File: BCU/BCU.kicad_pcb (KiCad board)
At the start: 2 copper layers, 73 parts, among them IC1 STM32G474RET6, IC2 TJA1042T_3,118, IC3 LM317MDCYR, IC4 LTC6820HUD#PBF, IC5 LM2842YQMK_NOPB, IC6 LM5164DDAR, J1 JTAG Connector, J2 SM04B-PASS-TBT_LF__SN_, J3 Conn_01x07_Male, J4 SM04B-PASS-TBT_LF__SN_, J5 SM04B-PASS-TBT_LF__SN_, J6 USB_C_Receptacle_USB2.0, SW1 SW_Push, T1 PE-68386NLT, Y1 NX2520SA-24.000000MHZ-B8

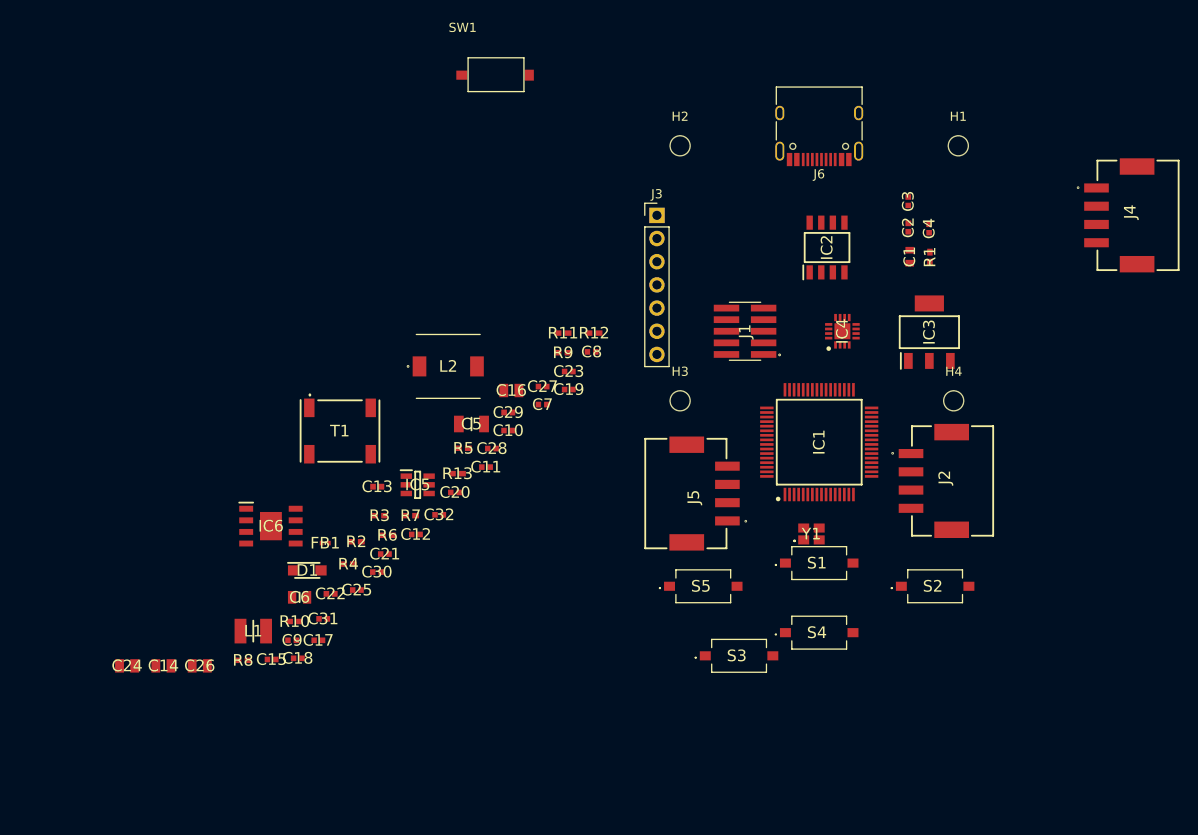
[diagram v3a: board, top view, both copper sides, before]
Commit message: Make rough component placement for evaluating missing 3D
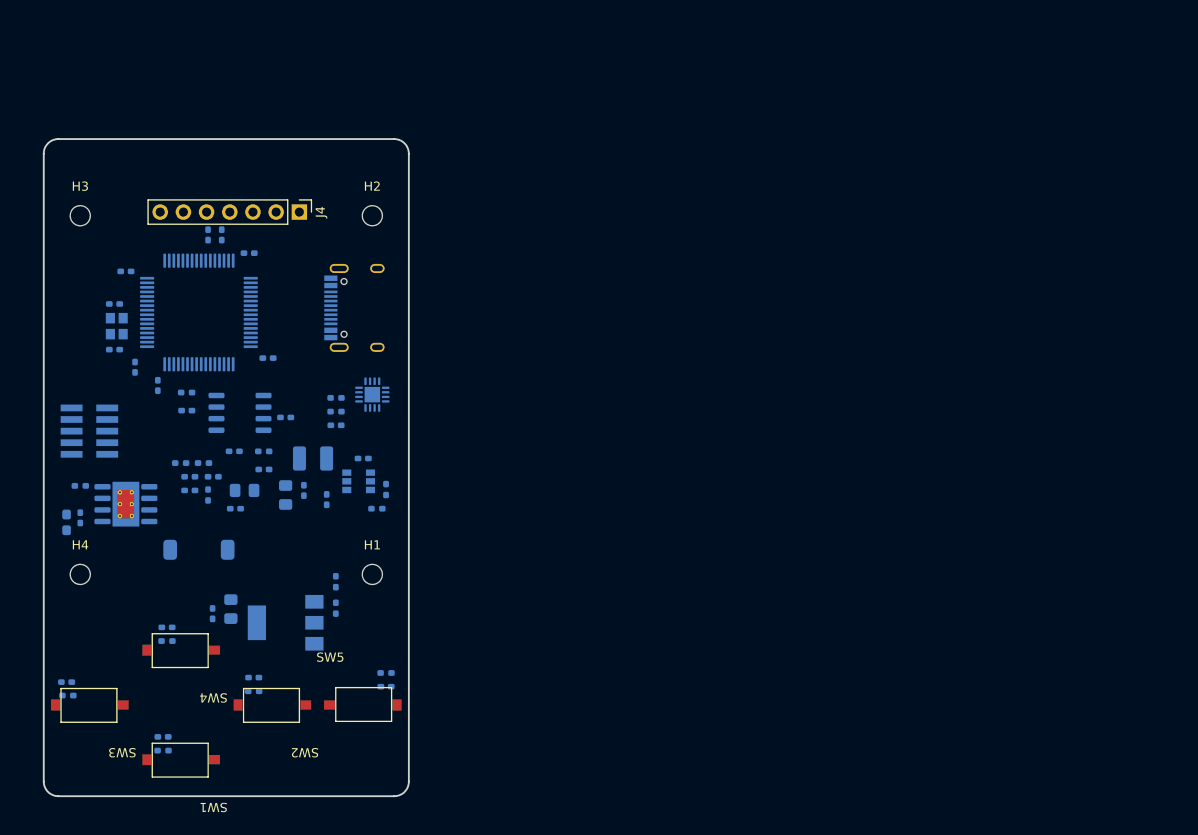
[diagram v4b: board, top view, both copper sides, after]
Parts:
- removed D1: MBR140SFT1G, SamacSys_Parts:SODFL3616X98N
- removed FB1: BLM15HD182SN1D, SamacSys_Parts:NFZ15SG152SN10B
- removed IC6: LM5164DDAR, SamacSys_Parts:SOIC127P600X170-9N
- removed J3: Conn_01x07_Male, Connector_PinHeader_2.54mm:PinHeader_1x07_P2.54mm_Vertical
- removed J5: SM04B-PASS-TBT_LF__SN_, SamacSys_Parts:SM04B-PASS-TBT
- removed J6: USB_C_Receptacle_USB2.0, Connector_USB:USB_C_Receptacle_HRO_TYPE-C-31-M-12
- removed S1, S2, S3, S4, S5: TS-1101-C-W, SamacSys_Parts:TS1101CW
- removed T1: PE-68386NLT, SamacSys_Parts:PE68386NLT
- added R14: 100K, Resistor_SMD:R_0402_1005Metric_Pad0.72x0.64mm_HandSolder, B.Cu at (140.5, 136.5)
- added R15: 100K, Resistor_SMD:R_0402_1005Metric_Pad0.72x0.64mm_HandSolder, B.Cu at (116.5, 133.0)
- added R16: 100K, Resistor_SMD:R_0402_1005Metric_Pad0.72x0.64mm_HandSolder, B.Cu at (126.0, 138.5)
- added R17: 100K, Resistor_SMD:R_0402_1005Metric_Pad0.72x0.64mm_HandSolder, B.Cu at (105.6, 139.0)
- added SW2: TS1101CW, coilchain-switch:TS-1101-C-W, F.Cu at (128.0, 140.0)
- added SW3: TS1101CW, coilchain-switch:TS-1101-C-W, F.Cu at (108.0, 140.0)
- added SW4: TS1101CW, coilchain-switch:TS-1101-C-W, F.Cu at (118.0, 134.0)
- added SW5: TS1101CW, coilchain-switch:TS-1101-C-W, F.Cu at (138.0, 140.0)
- added U1: LM317_SOT-223, Package_TO_SOT_SMD:SOT-223-3_TabPin2, B.Cu at (129.5, 131.0)
- C1: value 10V 10UF X5R -> 4.7uF; footprint SamacSys_Parts:CAPC1608X90N -> Capacitor_SMD:C_0603_1608Metric_Pad1.08x0.95mm_HandSolder; moved to B.Cu
- C10, C18, C19, C20, C21, C23, C25, C27, C3: value 16V 100NF X7R -> 100nF; footprint SamacSys_Parts:CAPC1005X55N -> Capacitor_SMD:C_0402_1005Metric_Pad0.74x0.62mm_HandSolder; moved to B.Cu
- C11: value 50V 3.3nF X7R ±10% 0402 -> 22uF; footprint SamacSys_Parts:CAPC1005X55N -> Capacitor_SMD:C_0805_2012Metric_Pad1.18x1.45mm_HandSolder; moved to B.Cu
- C12, C7: value 16V 100NF X7R -> 3.3nF; footprint SamacSys_Parts:CAPC1005X55N -> Capacitor_SMD:C_0402_1005Metric_Pad0.74x0.62mm_HandSolder; moved to B.Cu
- C13, C2, C22: value 25V 1UF X5R -> 100nF; footprint SamacSys_Parts:CAPC1005X60N -> Capacitor_SMD:C_0402_1005Metric_Pad0.74x0.62mm_HandSolder; moved to B.Cu
- C14: value 22uF+/-20% 25V X5R 0805 -> 22uF; footprint SamacSys_Parts:CAPC2012X145N -> Capacitor_SMD:C_0805_2012Metric_Pad1.18x1.45mm_HandSolder; moved to B.Cu
- C15: value 50V 56pF NP0 ±2% 0402 -> 100nF; footprint SamacSys_Parts:CAPC1005X55N -> Capacitor_SMD:C_0402_1005Metric_Pad0.74x0.62mm_HandSolder; moved to B.Cu
- C16: value 22uF+/-20% 25V X5R 0805 -> 10nF; footprint SamacSys_Parts:CAPC2012X145N -> Capacitor_SMD:C_0402_1005Metric_Pad0.74x0.62mm_HandSolder; moved to B.Cu
- C17: value 50V 3.3nF X7R ±10% 0402 -> 10nF; footprint SamacSys_Parts:CAPC1005X55N -> Capacitor_SMD:C_0402_1005Metric_Pad0.74x0.62mm_HandSolder; moved to B.Cu
- C24, C26: value 22uF+/-20% 25V X5R 0805 -> 100nF; footprint SamacSys_Parts:CAPC2012X145N -> Capacitor_SMD:C_0402_1005Metric_Pad0.74x0.62mm_HandSolder; moved to B.Cu
- C28, C30, C31, C32: value 16V 100NF X7R -> 10nF; footprint SamacSys_Parts:CAPC1005X55N -> Capacitor_SMD:C_0402_1005Metric_Pad0.74x0.62mm_HandSolder; moved to B.Cu
- C29: value 25V 1UF X5R -> 10nF; footprint SamacSys_Parts:CAPC1005X60N -> Capacitor_SMD:C_0402_1005Metric_Pad0.74x0.62mm_HandSolder; moved to B.Cu
- C4: value 50V 10PF C0G -> 100nF; footprint SamacSys_Parts:CAPC1005X55N -> Capacitor_SMD:C_0402_1005Metric_Pad0.74x0.62mm_HandSolder; moved to B.Cu
- C5: value 100V 4.7uF X7S ±10% 1206 -> 100nF; footprint SamacSys_Parts:CAPC3216X180N -> Capacitor_SMD:C_0402_1005Metric_Pad0.74x0.62mm_HandSolder; moved to B.Cu
- C6: value 100V 100nF X7R ±10% 0805 -> 100nF; footprint SamacSys_Parts:CAPC2012X135N -> Capacitor_SMD:C_0402_1005Metric_Pad0.74x0.62mm_HandSolder; moved to B.Cu
- C8: value 16V 100NF X7R -> 22uF; footprint SamacSys_Parts:CAPC1005X55N -> Capacitor_SMD:C_0805_2012Metric_Pad1.18x1.45mm_HandSolder; moved to B.Cu
- C9: value 50V 10PF C0G -> 56pF; footprint SamacSys_Parts:CAPC1005X55N -> Capacitor_SMD:C_0402_1005Metric_Pad0.74x0.62mm_HandSolder; moved to B.Cu
- IC1: value STM32G474RET6 -> LM2842YQMK_NOPB; footprint SamacSys_Parts:QFP50P1200X1200X160-64N -> Package_TO_SOT_SMD:SuperSOT-6; moved to B.Cu
- IC2: value TJA1042T_3,118 -> LM5164DDAR; footprint SamacSys_Parts:SOIC127P600X175-8N -> Package_SO:Texas_R-PDSO-G8_EP2.95x4.9mm_Mask2.4x3.1mm_ThermalVias; moved to B.Cu
- IC3: value LM317MDCYR -> STM32G474RET6; footprint SamacSys_Parts:SOT230P700X180-4N -> Package_QFP:LQFP-64_10x10mm_P0.5mm; moved to B.Cu
- IC4: value LTC6820HUD#PBF -> TJA1042T; footprint SamacSys_Parts:QFN50P300X300X80-17N-D -> Package_SO:SO-8_3.9x4.9mm_P1.27mm; moved to B.Cu
- IC5: value LM2842YQMK_NOPB -> LTC6820HUD#PBF; footprint SamacSys_Parts:SOT95P280X110-6N -> Package_DFN_QFN:QFN-16-1EP_3x3mm_P0.5mm_EP1.7x1.7mm; moved to B.Cu
- J1: value JTAG Connector -> USB_C_Receptacle_USB2.0; footprint SamacSys_Parts:FTSH-105-XX-YYY-DV-K-P-TR -> Connector_USB:USB_C_Receptacle_HRO_TYPE-C-31-M-12; moved to B.Cu
- J2: value SM04B-PASS-TBT_LF__SN_ -> JTAG; footprint SamacSys_Parts:SM04B-PASS-TBT -> Connector_PinHeader_1.27mm:PinHeader_2x05_P1.27mm_Vertical_SMD; moved to B.Cu
- J4: value SM04B-PASS-TBT_LF__SN_ -> Conn_01x07_Male; footprint SamacSys_Parts:SM04B-PASS-TBT -> Connector_PinHeader_2.54mm:PinHeader_1x07_P2.54mm_Vertical
- L1: value CBC3225T680KRV -> 68uH; footprint SamacSys_Parts:INDC3225X270N -> Inductor_SMD:L_1210_3225Metric_Pad1.42x2.65mm_HandSolder; moved to B.Cu
- L2: value SLF7045T-680MR60-PF -> 68uH; footprint SamacSys_Parts:SLF7032_7045 -> Inductor_SMD:L_TDK_SLF7045; moved to B.Cu
- R1: value 100K 1% 1/16W 0402 -> 100K; footprint SamacSys_Parts:RESC1005X40N -> Resistor_SMD:R_0402_1005Metric_Pad0.72x0.64mm_HandSolder; moved to B.Cu
- R10, R11, R12: value 51R 1% 1/16W 0402 -> 51R; footprint SamacSys_Parts:RESC1005X40N -> Resistor_SMD:R_0402_1005Metric_Pad0.72x0.64mm_HandSolder; moved to B.Cu
- R13: value 51R 1% 1/16W 0402 -> 100K; footprint SamacSys_Parts:RESC1005X40N -> Resistor_SMD:R_0402_1005Metric_Pad0.72x0.64mm_HandSolder; moved to B.Cu
- R2: value 10K 1% 1/16W 0402 -> 8.2K; footprint SamacSys_Parts:RESC1005X40N -> Resistor_SMD:R_0402_1005Metric_Pad0.72x0.64mm_HandSolder; moved to B.Cu
- R3: value 1.5K 1% 1/16W 0402 -> 10K; footprint SamacSys_Parts:RESC1005X40N -> Resistor_SMD:R_0402_1005Metric_Pad0.72x0.64mm_HandSolder; moved to B.Cu
- R4: value 100K 1% 1/16W 0402 -> 1.5K; footprint SamacSys_Parts:RESC1005X40N -> Resistor_SMD:R_0402_1005Metric_Pad0.72x0.64mm_HandSolder; moved to B.Cu
- R5: value 8.2K 1% 1/16W 0402 -> 8.2K; footprint SamacSys_Parts:RESC1005X40N -> Resistor_SMD:R_0402_1005Metric_Pad0.72x0.64mm_HandSolder; moved to B.Cu
- R6: value 8.2K 1% 1/16W 0402 -> 453K; footprint SamacSys_Parts:RESC1005X40N -> Resistor_SMD:R_0402_1005Metric_Pad0.72x0.64mm_HandSolder; moved to B.Cu
- R7: value 453kΩ 1% 402 -> 453K; footprint SamacSys_Parts:RESC1005X40N -> Resistor_SMD:R_0402_1005Metric_Pad0.72x0.64mm_HandSolder; moved to B.Cu
- R8: value 453kΩ 1% 402 -> 49.9K; footprint SamacSys_Parts:RESC1005X40N -> Resistor_SMD:R_0402_1005Metric_Pad0.72x0.64mm_HandSolder; moved to B.Cu
- R9: value 49.9K 1% 1/16W 0402 -> 51R; footprint SamacSys_Parts:RESC1005X40N -> Resistor_SMD:R_0402_1005Metric_Pad0.72x0.64mm_HandSolder; moved to B.Cu
- SW1: value SW_Push -> TS1101CW
- Y1: value NX2520SA-24.000000MHZ-B8 -> NX2520SA; footprint SamacSys_Parts:NX2520SA24000000MHZB8 -> Crystal:Crystal_SMD_2520-4Pin_2.5x2.0mm; moved to B.Cu
- moved C4 98.3 mm to (107.0, 119.5)
- moved H4 97.6 mm to (107.0, 125.7)
- moved C1 96.9 mm to (105.5, 120.0)
- moved R1 96.4 mm to (107.0, 116.0), turned to 180 degrees
- moved J2 90.3 mm to (108.0, 110.0), turned to 0 degrees
- moved J4 87.4 mm to (131.0, 86.0)
- moved SW1 82.6 mm to (118.0, 146.0), turned to 180 degrees
- moved IC2 81.8 mm to (112.0, 118.0), turned to 0 degrees
- moved IC3 80.1 mm to (120.0, 97.0), turned to 0 degrees
- moved H1 79.5 mm to (139.0, 125.7)
- moved Y1 79.4 mm to (111.0, 98.5), turned to -90 degrees
- moved C3 72.2 mm to (129.5, 108.5), turned to 180 degrees
- moved C2 70.4 mm to (134.0, 117.5)
- moved H3 68.8 mm to (107.0, 86.4)
- moved IC4 66.6 mm to (124.5, 108.0), turned to 180 degrees
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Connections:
- C1 pad 2: +3V3 -> +48V
- C11 pad 1: Net-(C11-Pad1) -> GND
- C11 pad 2: Net-(C11-Pad2) -> +5V
- C12 pad 1: GND -> Net-(C12-Pad1)
- C12 pad 2: +3V3 -> +12V
- C13 pad 2: +5V -> +12V
- C14 pad 2: +5V -> +12V
- C15 pad 1: Net-(C15-Pad1) -> GND
- C15 pad 2: Net-(C15-Pad2) -> +3V3
- C16 pad 1: GND -> Net-(C16-Pad1)
- C16 pad 2: +5V -> GND
- C17 pad 1: Net-(C15-Pad2) -> GND
- C17 pad 2: +12V -> Net-(C17-Pad2)
- C2 pad 2: +3V3 -> +12V
- C20 pad 2: +12V -> +3V3
- C22 pad 2: +12V -> +3V3
- C24 pad 2: +12V -> +3V3
- C25 pad 2: +3V3 -> +5V
- C26 pad 2: +12V -> Net-(C26-Pad2)
- C27 pad 2: +5V -> Net-(C27-Pad2)
- C28 pad 2: +3.3VA -> /mcu/BTN_PWR
- C29 pad 2: +3.3VA -> /mcu/BTN_RIGHT
- C30 pad 2: +3V3 -> /mcu/BTN_LEFT
- C31 pad 2: Net-(C31-Pad2) -> /mcu/BTN_UP
- C32 pad 2: Net-(C32-Pad2) -> /mcu/BTN_DOWN
- C4 pad 2: Net-(C4-Pad2) -> +48V
- C5 pad 1: GND -> Net-(C5-Pad1)
- C6 pad 2: Net-(C5-Pad2) -> +3V3
- C7 pad 1: +12V -> Net-(C7-Pad1)
- C7 pad 2: GND -> Net-(C7-Pad2)
- C8 pad 1: Net-(C8-Pad1) -> GND
- C8 pad 2: Net-(C8-Pad2) -> +3V3
- C9 pad 1: GND -> Net-(C9-Pad1)
- C9 pad 2: Net-(C9-Pad2) -> Net-(C12-Pad1)
- IC1 pad 1: +3V3 -> Net-(C5-Pad1)
- IC1 pad 2: unconnected-(IC1-Pad2) -> GND
- IC1 pad 3: unconnected-(IC1-Pad3) -> Net-(R4-Pad1)
- IC1 pad 4: unconnected-(IC1-Pad4) -> +12V
- IC1 pad 5: Net-(C9-Pad2) -> +12V
- IC1 pad 6: Net-(C4-Pad2) -> Net-(C5-Pad2)
- IC2 pad 1: Net-(IC1-Pad59) -> GND
- IC2 pad 2: GND -> +48V
- IC2 pad 3: +5V -> +48V
- IC2 pad 4: Net-(IC1-Pad60) -> Net-(R1-Pad1)
- IC2 pad 5: +3V3 -> Net-(C9-Pad1)
- IC2 pad 6: Net-(IC2-Pad6) -> unconnected-(IC2-Pad6)
- IC2 pad 7: Net-(IC2-Pad7) -> Net-(C7-Pad1)
- IC2 pad 8: GND -> Net-(C7-Pad2)
- IC3 pad 1: Net-(IC3-Pad1) -> +3V3
- IC3 pad 2: +3V3 -> unconnected-(IC3-Pad2)
- IC3 pad 3: +5V -> unconnected-(IC3-Pad3)
- IC3 pad 4: +3V3 -> unconnected-(IC3-Pad4)
- IC4 pad 1: Net-(IC1-Pad37) -> /can/CAN_TXD
- IC4 pad 2: Net-(IC1-Pad36) -> GND
- IC4 pad 3: Net-(IC1-Pad35) -> +5V
- IC4 pad 4: Net-(IC1-Pad34) -> /can/CAN_RXD
- IC4 pad 5: unconnected-(IC4-Pad5) -> +3V3
- IC4 pad 6: unconnected-(IC4-Pad6) -> Net-(IC4-Pad6)
- IC4 pad 7: unconnected-(IC4-Pad7) -> Net-(IC4-Pad7)
- IC4 pad 8: unconnected-(IC4-Pad8) -> /can/CAN_STB
- IC5 pad 1: Net-(C8-Pad2) -> /battery/BATT_MOSI
- IC5 pad 2: GND -> /battery/BATT_MISO
- IC5 pad 3: Net-(IC5-Pad3) -> /battery/BATT_SCK
- IC5 pad 4: +12V -> /battery/BATT_nCS
- IC5 pad 5: +12V -> unconnected-(IC5-Pad5)
- IC5 pad 6: Net-(C8-Pad1) -> unconnected-(IC5-Pad6)
- J2 pad 1: +12V -> +3V3
- J2 pad 2: unconnected-(J2-Pad2) -> /mcu/JTAG_TMS
- J2 pad 3: unconnected-(J2-Pad3) -> GND
- J2 pad 4: GND -> /mcu/JTAG_TCK
- J2 pad 5: (no net) -> GND
- J2 pad 6: (no net) -> /mcu/JTAG_TDO
- J4 pad 1: Net-(IC2-Pad7) -> +3V3
- J4 pad 2: Net-(IC2-Pad6) -> GND
- J4 pad 3: unconnected-(J4-Pad3) -> /mcu/OLED_DIN
- J4 pad 4: unconnected-(J4-Pad4) -> /mcu/OLED_CLK
- J4 pad 5: (no net) -> /mcu/OLED_CS
- J4 pad 6: (no net) -> /mcu/OLED_DC
- L1 pad 1: Net-(C8-Pad1) -> Net-(C5-Pad2)
- L2 pad 1: Net-(C11-Pad2) -> Net-(C7-Pad2)
- R1 pad 1: Net-(IC1-Pad61) -> Net-(R1-Pad1)
- R10 pad 1: Net-(IC2-Pad7) -> Net-(IC4-Pad7)
- R10 pad 2: Net-(C31-Pad2) -> Net-(C26-Pad2)
- R11 pad 1: Net-(IC4-Pad10) -> Net-(IC5-Pad9)
- R11 pad 2: Net-(C32-Pad2) -> Net-(C27-Pad2)
- R12 pad 1: Net-(IC2-Pad6) -> Net-(IC5-Pad10)
- R12 pad 2: Net-(C31-Pad2) -> Net-(C27-Pad2)
- R13 pad 1: Net-(IC4-Pad9) -> +3V3
- R13 pad 2: Net-(C32-Pad2) -> /mcu/BTN_PWR
- R2 pad 1: GND -> +3V3
- R2 pad 2: Net-(IC3-Pad1) -> Net-(R2-Pad2)
- R3 pad 1: Net-(IC5-Pad3) -> Net-(R2-Pad2)
- R4 pad 1: GND -> Net-(R4-Pad1)
- R4 pad 2: Net-(IC6-Pad4) -> GND
- R5 pad 1: +3V3 -> Net-(R4-Pad1)
- R5 pad 2: Net-(IC3-Pad1) -> +5V
- R6 pad 1: +5V -> Net-(C7-Pad2)
- R6 pad 2: Net-(IC5-Pad3) -> Net-(C12-Pad1)
- R7 pad 1: Net-(C15-Pad2) -> +12V
- R7 pad 2: Net-(C11-Pad2) -> Net-(C9-Pad1)
- R8 pad 1: Net-(C15-Pad1) -> Net-(C9-Pad1)
- R8 pad 2: +12V -> GND
- R9 pad 1: GND -> Net-(IC4-Pad6)
- R9 pad 2: Net-(C15-Pad1) -> Net-(C26-Pad2)
- SW1 pad 1: unconnected-(SW1-Pad1) -> GND
- SW1 pad 2: unconnected-(SW1-Pad2) -> /mcu/BTN_PWR
- Y1 pad 1: Net-(C9-Pad2) -> Net-(C17-Pad2)
- Y1 pad 3: Net-(C4-Pad2) -> Net-(C16-Pad1)
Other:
- board outline added: 40 x 72 mm
